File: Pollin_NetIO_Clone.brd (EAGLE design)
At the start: 109 x 76 mm, 62 parts, among them IC1 7805, IC2 LM317T, IC3 ENC28J60SP, IC4 MAX232, IC5 MEGA32-16PU, J1 MKDSN1,5/2-5,08, J10 MKDSN1,5/2-5,08, J2 74980111212, J3 618025231221, J5 618009231121, J6 MKDSN1,5/2-5,08, J7 MKDSN1,5/2-5,08, J8 MKDSN1,5/2-5,08, J9 MKDSN1,5/2-5,08, Q1 25MHz, Q2 16MHz

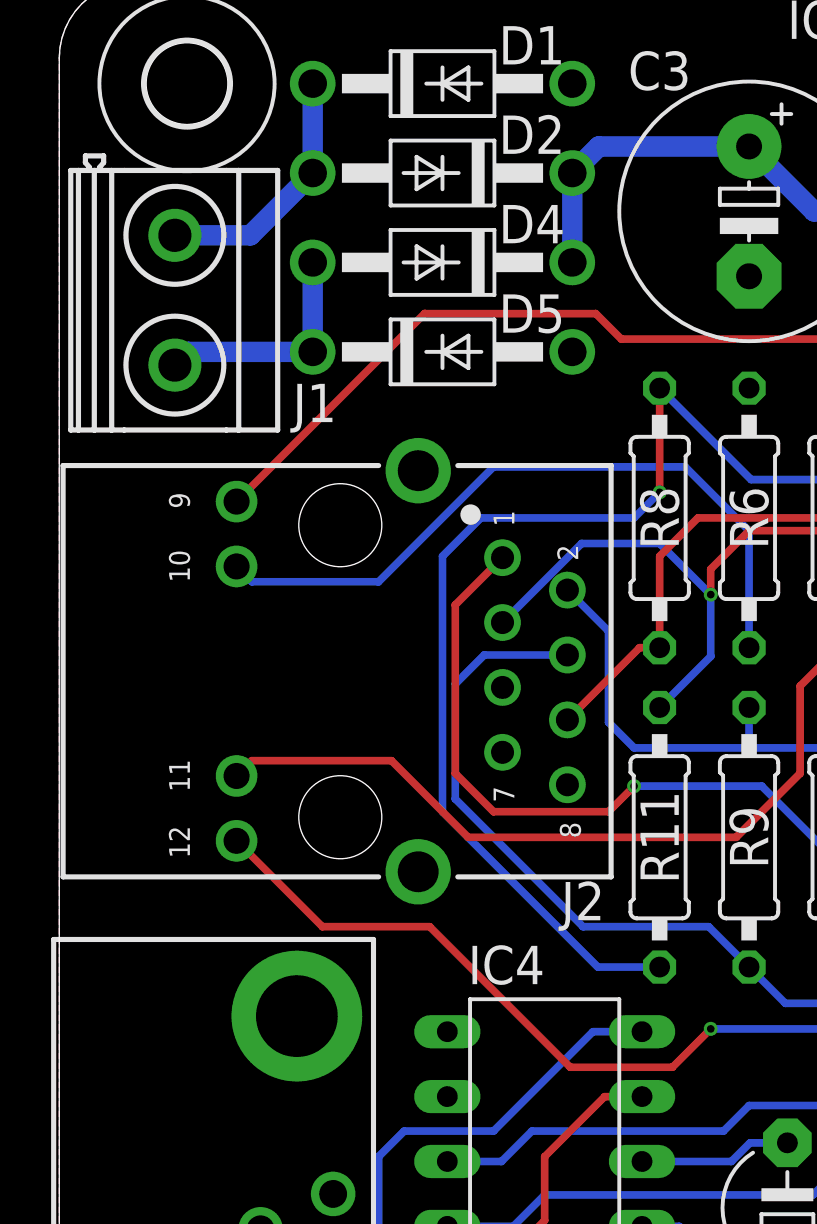
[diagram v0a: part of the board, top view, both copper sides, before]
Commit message: * cleanded up schematic * changed RJ45 connector to something compatible with the original one
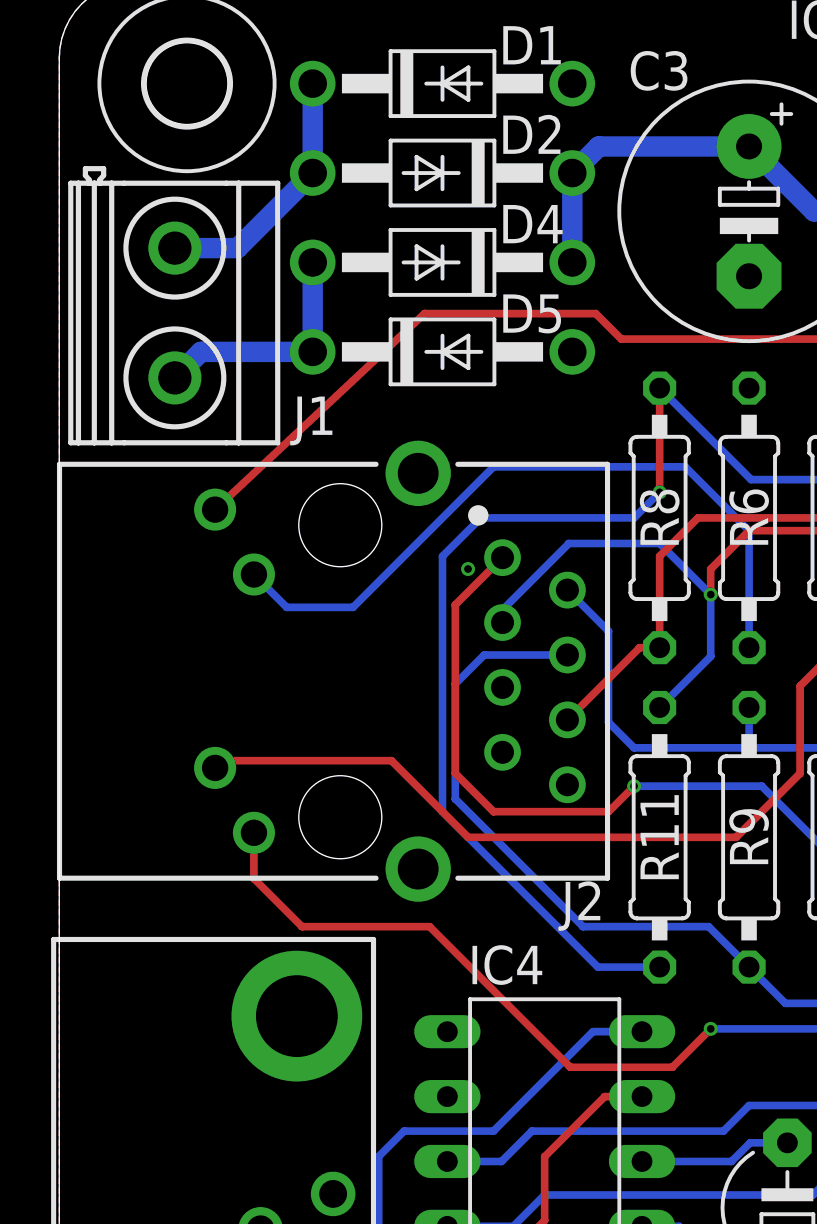
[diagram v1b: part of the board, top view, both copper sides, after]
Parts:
- J2: value 74980111212 -> 7499010211A; device Wurth_Signal & Communications_WE-RJ45_LAN:74980111212 -> Wurth_Signal & Communications_WE-RJ45_LAN:7499010211A
- moved J1 0.50 mm to (4.50, 63.0)
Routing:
- net LEDA: track 79.2 -> 80.1 mm
- net N$38: track 30.1 -> 30.8 mm
- net LEDB: track 73.4 -> 73.9 mm
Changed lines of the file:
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@@
 <attribute name="VALUE" x="32.571" y="53.706" locked="yes" size="1.27" layer="27" ratio="10"/>
 </element>
-<element name="J2" library="Wurth_Signal &amp; Communications_WE-RJ45_LAN" library_urn="urn:adsk.eagle:library:14284239" package="74980111212" package3d_urn="urn:adsk.eagle:package:30734208/5" value=" 74980111212 " x="11" y="49" smashed="yes" rot="R270">
-<attribute name="DATA-RATE" value="10/100BASE-T" x="11" y="49" size="1" layer="27" rot="R270" display="off"/>
-<attribute name="DATASHEET-URL" value="https://www.we-online.com/redexpert/spec/74980111212?ae" x="11" y="49" size="1" layer="27" rot="R270" display="off"/>
-<attribute name="LED" value="yellow-green" x="11" y="49" size="1" layer="27" rot="R270" display="off"/>
+<element name="J2" library="Wurth_Signal &amp; Communications_WE-RJ45_LAN" library_urn="urn:adsk.eagle:library:14284239" package="7499010211A" package3d_urn="urn:adsk.eagle:package:12863510/4" value="7499010211A" x="11" y="49" smashed="yes" rot="R270">
+<attribute name="DATA-RATE" value="10/100 Base-T" x="11" y="49" size="1" layer="27" rot="R270" display="off"/>
+<attribute name="DATASHEET-URL" value="https://www.we-online.com/redexpert/spec/7499010211A?ae" x="11" y="49" size="1" layer="27" rot="R270" display="off"/>
+<attribute name="LED" value="green-yellow" x="11" y="49" size="1" layer="27" rot="R270" display="off"/>
 <attribute name="MOUNT" value="THT" x="11" y="49" size="1" layer="27" rot="R270" display="off"/>
 <attribute name="NAME" x="20.5" y="40" size="1.5" layer="25" font="vector" ratio="12" rot="R180" align="center"/>
-<attribute name="PART-NUMBER" value=" 74980111212 " x="11" y="49" size="1" layer="27" rot="R270" display="off"/>
+<attribute name="PART-NUMBER" value="7499010211A" x="11" y="49" size="1" layer="27" rot="R270" display="off"/>
 <attribute name="POE" value="non-PoE" x="11" y="49" size="1" layer="27" rot="R270" display="off"/>
 <attribute name="PORTS" value=" 1 " x="11" y="49" size="1" layer="27" rot="R270" display="off"/>
 <attribute name="USB" value="No" x="11" y="49" size="1" layer="27" rot="R270" display="off"/>
-<attribute name="VALUE" x="-2" y="49" size="1.27" layer="51" rot="R270" align="bottom-center"/>
+<attribute name="VALUE" value="7499010211A" x="-2" y="49" size="1.27" layer="51" rot="R270" align="bottom-center"/>
 </element>
 <element name="J11" library="jumper" library_urn="urn:adsk.eagle:library:252" package="JP2" package3d_urn="urn:adsk.eagle:package:15452/1" value="" x="89" y="47.5" smashed="yes" rot="R180">
@@
 <attribute name="VALUE" x="92.556" y="51.818" size="1.27" layer="27" ratio="10" rot="R180"/>
 </element>
-<element name="J1" library="con-phoenix-508" library_urn="urn:adsk.eagle:library:176" package="MKDSN1,5/2-5,08" package3d_urn="urn:adsk.eagle:package:9630/1" value="MKDSN1,5/2-5,08" x="4.5" y="63.5" smashed="yes" rot="R270">
-<attribute name="NAME" x="10" y="59.5" size="1.5" layer="25" font="vector" ratio="12" align="center"/>
-<attribute name="POPULARITY" value="14" x="4.5" y="63.5" size="1" layer="27" rot="R270" display="off"/>
-<attribute name="VALUE" x="0.69" y="56.515" size="1.27" layer="27"/>
+<element name="J1" library="con-phoenix-508" library_urn="urn:adsk.eagle:library:176" package="MKDSN1,5/2-5,08" package3d_urn="urn:adsk.eagle:package:9630/1" value="MKDSN1,5/2-5,08" x="4.5" y="63" smashed="yes" rot="R270">
+<attribute name="NAME" x="10" y="59" size="1.5" layer="25" font="vector" ratio="12" align="center"/>
+<attribute name="POPULARITY" value="14" x="4.5" y="63" size="1" layer="27" rot="R270" display="off"/>
+<attribute name="VALUE" x="0.69" y="56.015" size="1.27" layer="27"/>
 </element>
 <element name="J10" library="con-phoenix-508" library_urn="urn:adsk.eagle:library:176" package="MKDSN1,5/2-5,08" package3d_urn="urn:adsk.eagle:package:9630/1" value="MKDSN1,5/2-5,08" x="80.28" y="4.58" smashed="yes">
@@
 <vertex x="0" y="3"/>
 </polygon>
+<via x="16" y="53" extent="1-16" drill="0.3"/>
 </signal>
 <signal name="N$1">
@@
 <contactref element="D2" pad="A"/>
 <contactref element="J1" pad="1"/>
-<wire x1="4.525" y1="66.0611" x2="7.4811" y2="66.0611" width="0.8" layer="16"/>
-<wire x1="7.4811" y1="66.0611" x2="9.92" y2="68.5" width="0.8" layer="16"/>
+<wire x1="4.525" y1="65.5611" x2="6.9811" y2="65.5611" width="0.8" layer="16"/>
+<wire x1="6.9811" y1="65.5611" x2="9.92" y2="68.5" width="0.8" layer="16"/>
 <wire x1="9.92" y1="68.5" x2="9.92" y2="72" width="0.8" layer="16"/>
 </signal>
@@
 <contactref element="D5" pad="C"/>
 <contactref element="J1" pad="2"/>
-<wire x1="4.525" y1="60.9811" x2="5.0439" y2="61.5" width="0.8" layer="16"/>
-<wire x1="5.0439" y1="61.5" x2="9.92" y2="61.5" width="0.8" layer="16"/>
+<wire x1="4.525" y1="60.4811" x2="5.5439" y2="61.5" width="0.8" layer="16"/>
+<wire x1="5.5439" y1="61.5" x2="9.92" y2="61.5" width="0.8" layer="16"/>
 <wire x1="9.92" y1="61.5" x2="9.92" y2="65" width="0.8" layer="16"/>
 </signal>
@@
 <via x="25.5" y="52" extent="1-16" drill="0.3"/>
 <wire x1="25.5" y1="52" x2="23.5" y2="54" width="0.3" layer="16"/>
-<wire x1="20.445" y1="54" x2="17.35" y2="50.905" width="0.3" layer="16"/>
-<wire x1="23.5" y1="54" x2="20.445" y2="54" width="0.3" layer="16"/>
+<wire x1="19.945" y1="54" x2="17.35" y2="51.405" width="0.3" layer="16"/>
+<wire x1="17.35" y1="51.405" x2="17.35" y2="50.905" width="0.3" layer="16"/>
+<wire x1="23.5" y1="54" x2="19.945" y2="54" width="0.3" layer="16"/>
 <wire x1="23.5" y1="47.58" x2="25.5" y2="49.58" width="0.3" layer="16"/>
 <wire x1="25.5" y1="49.58" x2="25.5" y2="52" width="0.3" layer="16"/>
@@
 <wire x1="50" y1="42.5" x2="48" y2="40.5" width="0.3" layer="16"/>
 <wire x1="37" y1="40.5" x2="48" y2="40.5" width="0.3" layer="16"/>
-<wire x1="6.94" y1="42.36" x2="10.3" y2="39" width="0.3" layer="1"/>
-<wire x1="10.3" y1="39" x2="14.5" y2="39" width="0.3" layer="1"/>
-<wire x1="14.5" y1="39" x2="20" y2="33.5" width="0.3" layer="1"/>
+<wire x1="20" y1="33.5" x2="14.5" y2="39" width="0.3" layer="1"/>
 <wire x1="24" y1="33.5" x2="25.5" y2="35" width="0.3" layer="1"/>
 <via x="25.5" y="35" extent="1-16" drill="0.3"/>
@@
 <wire x1="20" y1="33.5" x2="24" y2="33.5" width="0.3" layer="1"/>
 <wire x1="31.5" y1="35" x2="37" y2="40.5" width="0.3" layer="16"/>
+<wire x1="7.62" y1="40.88" x2="7.62" y2="42.675" width="0.3" layer="1"/>
+<wire x1="14.5" y1="39" x2="9.5" y2="39" width="0.3" layer="1"/>
+<wire x1="9.5" y1="39" x2="7.62" y2="40.88" width="0.3" layer="1"/>
 </signal>
 <signal name="LEDA">
 <contactref element="IC3" pad="27"/>
 <contactref element="J2" pad="9"/>
-<wire x1="6.94" y1="55.64" x2="14.3" y2="63" width="0.3" layer="1"/>
+<wire x1="6.1" y1="55.325" x2="14.3" y2="63" width="0.3" layer="1"/>
 <wire x1="14.3" y1="63" x2="21" y2="63" width="0.3" layer="1"/>
 <wire x1="21" y1="63" x2="22" y2="62" width="0.3" layer="1"/>
@@
 <wire x1="29" y1="48.42" x2="29" y2="45" width="0.3" layer="1"/>
 <wire x1="29" y1="45" x2="26.5" y2="42.5" width="0.3" layer="1"/>
-<wire x1="16" y1="42.5" x2="13" y2="45.5" width="0.3" layer="1"/>
-<wire x1="7.54" y1="45.5" x2="6.94" y2="44.9" width="0.3" layer="1"/>
-<wire x1="13" y1="45.5" x2="7.54" y2="45.5" width="0.3" layer="1"/>
+<wire x1="13" y1="45.5" x2="16" y2="42.5" width="0.3" layer="1"/>
+<wire x1="6.1" y1="45.215" x2="6.385" y2="45.5" width="0.3" layer="1"/>
+<wire x1="6.385" y1="45.5" x2="13" y2="45.5" width="0.3" layer="1"/>
 </signal>
 <signal name="N$39">
@@
 <wire x1="27" y1="54.5" x2="24.5" y2="57" width="0.3" layer="16"/>
 <wire x1="24.5" y1="57" x2="17" y2="57" width="0.3" layer="16"/>
-<wire x1="17" y1="57" x2="12.5" y2="52.5" width="0.3" layer="16"/>
-<wire x1="12.5" y1="52.5" x2="7.54" y2="52.5" width="0.3" layer="16"/>
-<wire x1="7.54" y1="52.5" x2="6.94" y2="53.1" width="0.3" layer="16"/>
+<wire x1="8.905" y1="51.5" x2="7.62" y2="52.785" width="0.3" layer="16"/>
+<wire x1="17" y1="57" x2="11.5" y2="51.5" width="0.3" layer="16"/>
+<wire x1="11.5" y1="51.5" x2="8.905" y2="51.5" width="0.3" layer="16"/>
 </signal>
 </signals>
@@
 <mfgpreviewcolor name="substratecolor" color="0xFF786E46"/>
 </mfgpreviewcolors>
+<errors>
+</errors>
 </board>
 </drawing>
